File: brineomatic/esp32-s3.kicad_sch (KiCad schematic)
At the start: 37 parts, among them J19 USB_TYPE_C_16PIN, J20 Conn_01x04, U5 ESP32-S3-WROOM-1-N16R8, U6 USBLC6-2SC6, U7 LDL1117S33R, U8 SN74LV1T34DBV

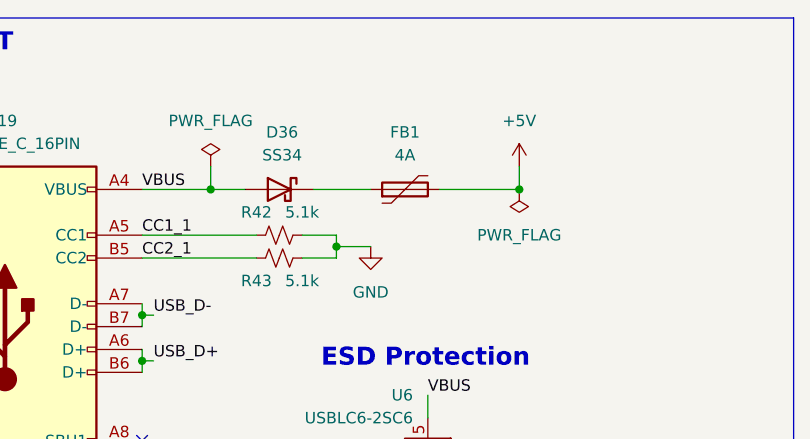
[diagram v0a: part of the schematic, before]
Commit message: change to 1.5A fuse on usb
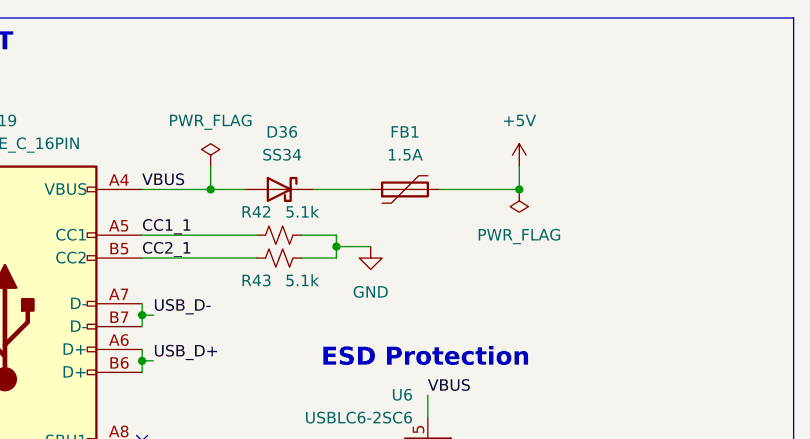
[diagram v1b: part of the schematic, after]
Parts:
- FB1: value 4A -> 1.5A; LCSC C2760306 -> C70083
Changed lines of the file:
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@@
 			)
 		)
-		(property "Value" "4A"
+		(property "Value" "1.5A"
 			(at 113.03 31.75 90)
 			(effects
@@
 			)
 		)
-		(property "LCSC" "C2760306"
+		(property "LCSC" "C70083"
 			(at 113.03 35.56 90)
 			(effects

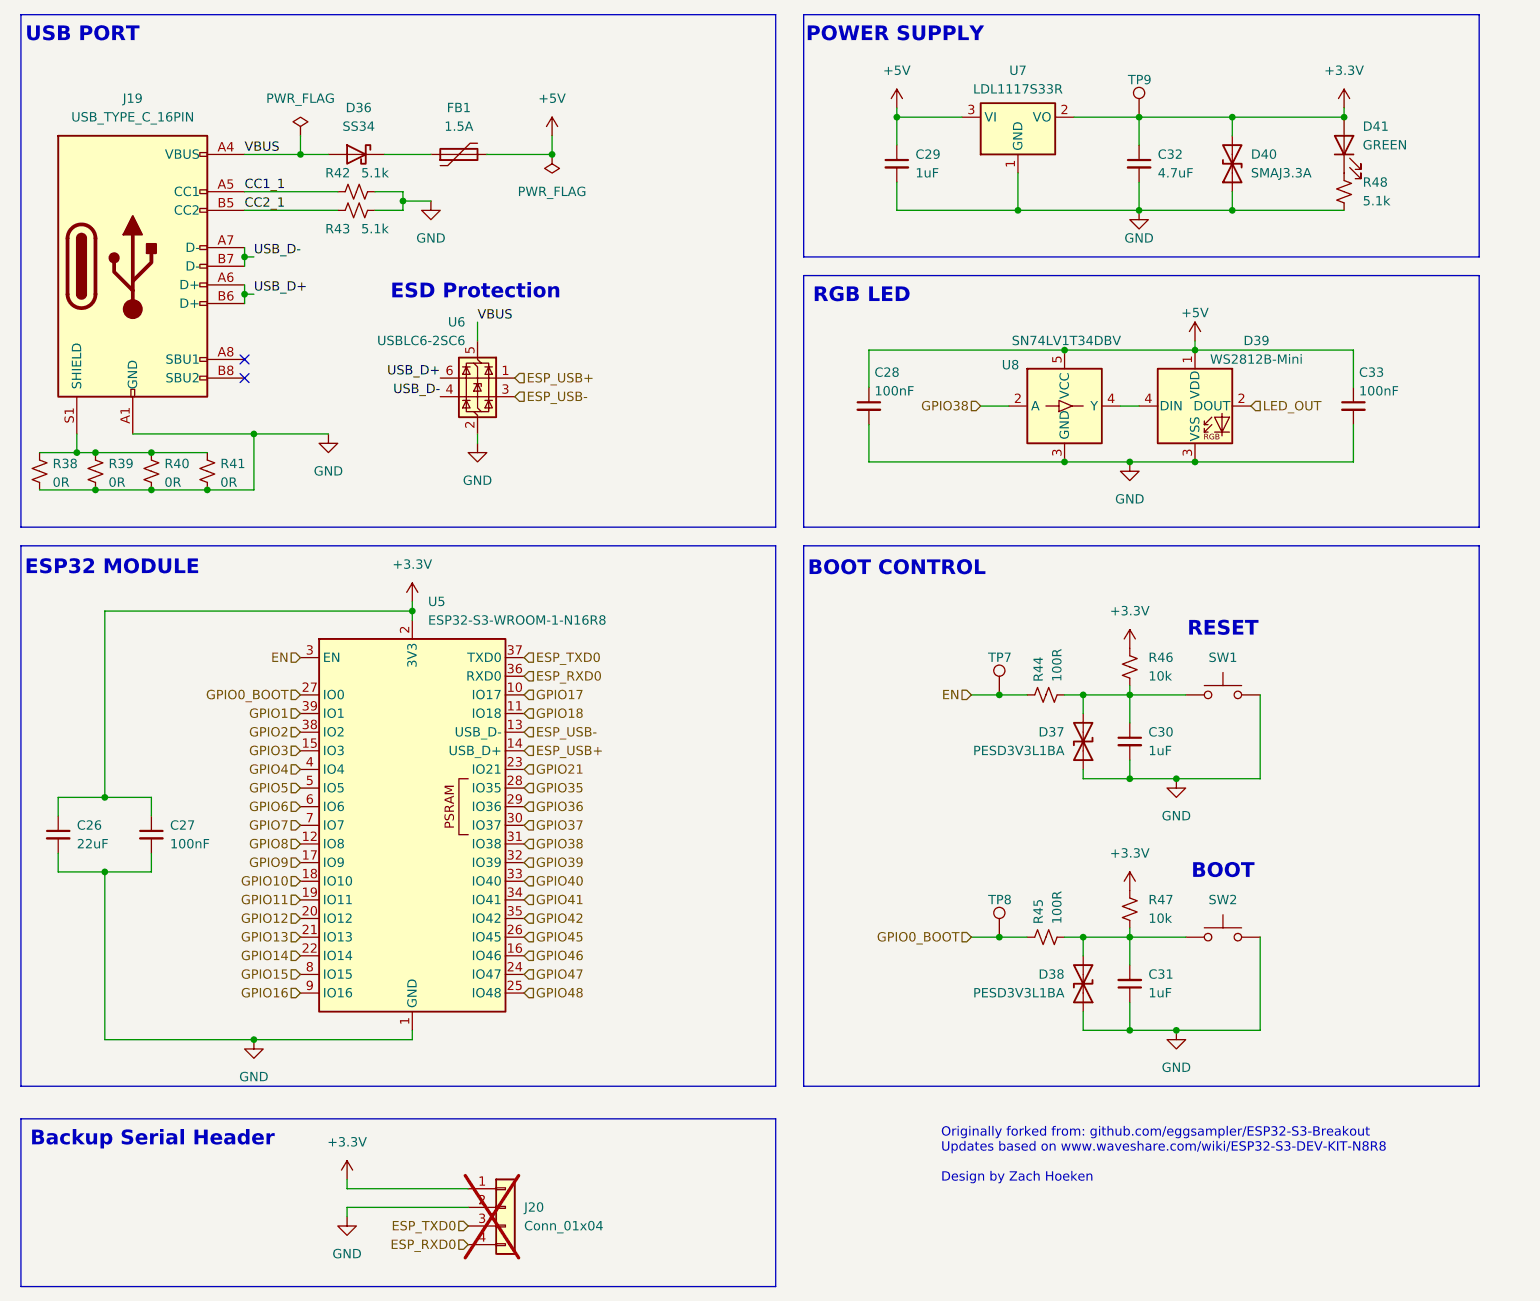
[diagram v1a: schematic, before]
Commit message: add inline resistor to temperature sensor + servo inputs - 100ohm
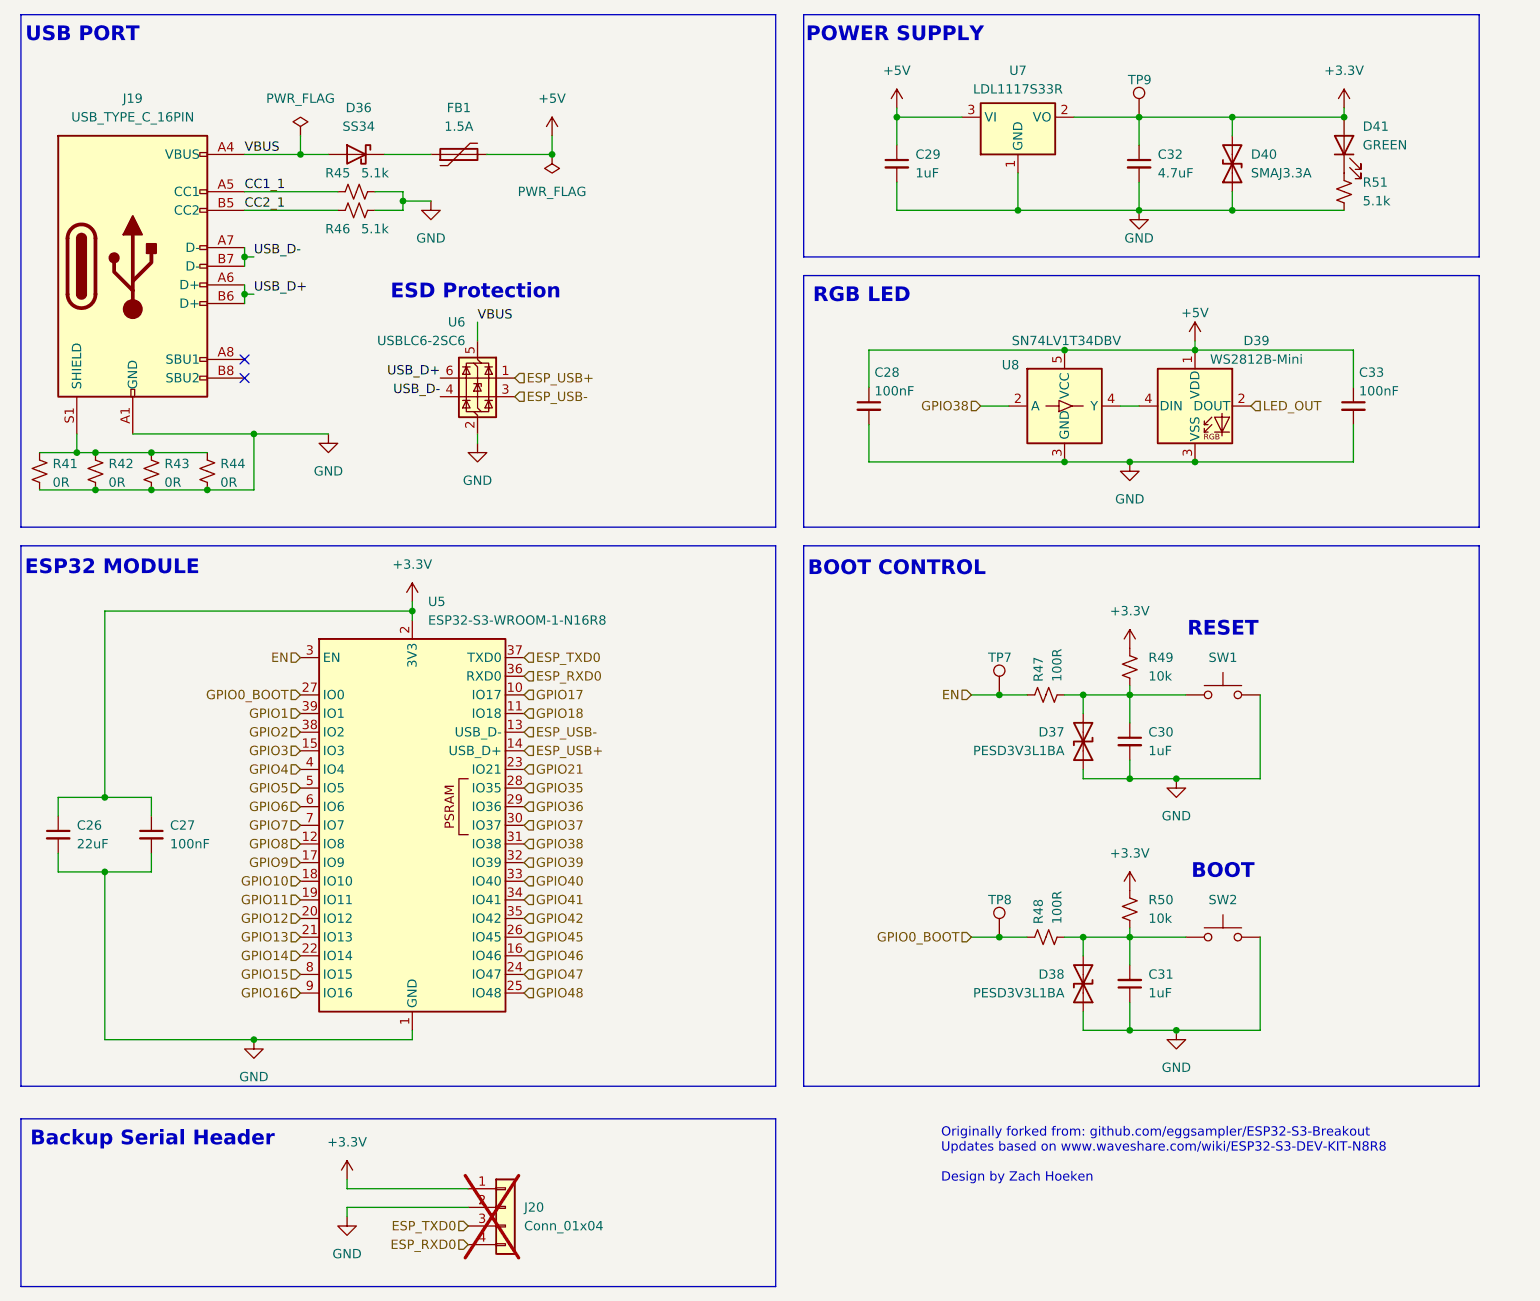
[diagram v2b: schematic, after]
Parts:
- renumbered R38 to R41, R39 to R42, R40 to R43, R41 to R44, R42 to R45, R43 to R46, R44 to R47, R45 to R48, R46 to R49, R47 to R50, R48 to R51
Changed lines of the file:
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@@
 		(on_board yes)
 		(dnp no)
-		(property "Reference" "R45"
+		(property "Reference" "R48"
 			(at 192.024 140.462 0)
 			(effects
@@
 			(project "brineomatic"
 				(path "/96477ae2-ef08-48f3-8dd4-fe4478541f68/602af921-0504-453c-a784-e82800e98f4c"
-					(reference "R45")
+					(reference "R48")
 					(unit 1)
 				)
@@
 		(on_board yes)
 		(dnp no)
-		(property "Reference" "R43"
+		(property "Reference" "R46"
 			(at 96.52 45.72 90)
 			(effects
@@
 			(project "brineomatic"
 				(path "/96477ae2-ef08-48f3-8dd4-fe4478541f68/602af921-0504-453c-a784-e82800e98f4c"
-					(reference "R43")
+					(reference "R46")
 					(unit 1)
 				)
@@
 		(on_board yes)
 		(dnp no)
-		(property "Reference" "R40"
+		(property "Reference" "R43"
 			(at 72.898 77.724 0)
 			(effects
@@
 			(project "brineomatic"
 				(path "/96477ae2-ef08-48f3-8dd4-fe4478541f68/602af921-0504-453c-a784-e82800e98f4c"
-					(reference "R40")
+					(reference "R43")
 					(unit 1)
 				)
@@
 		(on_board yes)
 		(dnp no)
-		(property "Reference" "R39"
+		(property "Reference" "R42"
 			(at 65.278 77.724 0)
 			(effects
@@
 			(project "brineomatic"
 				(path "/96477ae2-ef08-48f3-8dd4-fe4478541f68/602af921-0504-453c-a784-e82800e98f4c"
-					(reference "R39")
+					(reference "R42")
 					(unit 1)
 				)
@@
 		(on_board yes)
 		(dnp no)
-		(property "Reference" "R41"
+		(property "Reference" "R44"
 			(at 80.518 77.724 0)
 			(effects
@@
 			(project "brineomatic"
 				(path "/96477ae2-ef08-48f3-8dd4-fe4478541f68/602af921-0504-453c-a784-e82800e98f4c"
-					(reference "R41")
+					(reference "R44")
 					(unit 1)
 				)
@@
 		(on_board yes)
 		(dnp no)
-		(property "Reference" "R44"
+		(property "Reference" "R47"
 			(at 192.024 107.442 0)
 			(effects
@@
 			(project "brineomatic"
 				(path "/96477ae2-ef08-48f3-8dd4-fe4478541f68/602af921-0504-453c-a784-e82800e98f4c"
-					(reference "R44")
+					(reference "R47")
 					(unit 1)
 				)
@@
 		(dnp no)
 		(fields_autoplaced yes)
-		(property "Reference" "R47"
+		(property "Reference" "R50"
 			(at 207.01 137.1599 0)
 			(effects
@@
 			(project "brineomatic"
 				(path "/96477ae2-ef08-48f3-8dd4-fe4478541f68/602af921-0504-453c-a784-e82800e98f4c"
-					(reference "R47")
+					(reference "R50")
 					(unit 1)
 				)
@@
 		(on_board yes)
 		(dnp no)
-		(property "Reference" "R42"
+		(property "Reference" "R45"
 			(at 96.52 38.1 90)
 			(effects
@@
 			(project "brineomatic"
 				(path "/96477ae2-ef08-48f3-8dd4-fe4478541f68/602af921-0504-453c-a784-e82800e98f4c"
-					(reference "R42")
+					(reference "R45")
 					(unit 1)
 				)
@@
 		(on_board yes)
 		(dnp no)
-		(property "Reference" "R38"
+		(property "Reference" "R41"
 			(at 57.658 77.724 0)
 			(effects
@@
 			(project "brineomatic"
 				(path "/96477ae2-ef08-48f3-8dd4-fe4478541f68/602af921-0504-453c-a784-e82800e98f4c"
-					(reference "R38")
+					(reference "R41")
 					(unit 1)
 				)
@@
 		(dnp no)
 		(fields_autoplaced yes)
-		(property "Reference" "R48"
+		(property "Reference" "R51"
 			(at 236.22 39.3699 0)
 			(effects
@@
 			(project "brineomatic"
 				(path "/96477ae2-ef08-48f3-8dd4-fe4478541f68/602af921-0504-453c-a784-e82800e98f4c"
-					(reference "R48")
+					(reference "R51")
 					(unit 1)
 				)
@@
 		(dnp no)
 		(fields_autoplaced yes)
-		(property "Reference" "R46"
+		(property "Reference" "R49"
 			(at 207.01 104.1399 0)
 			(effects
@@
 			(project "brineomatic"
 				(path "/96477ae2-ef08-48f3-8dd4-fe4478541f68/602af921-0504-453c-a784-e82800e98f4c"
-					(reference "R46")
+					(reference "R49")
 					(unit 1)
 				)
